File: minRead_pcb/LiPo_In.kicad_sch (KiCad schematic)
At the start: 2 parts, among them J5 Conn_01x02, Q3 IRLML6402

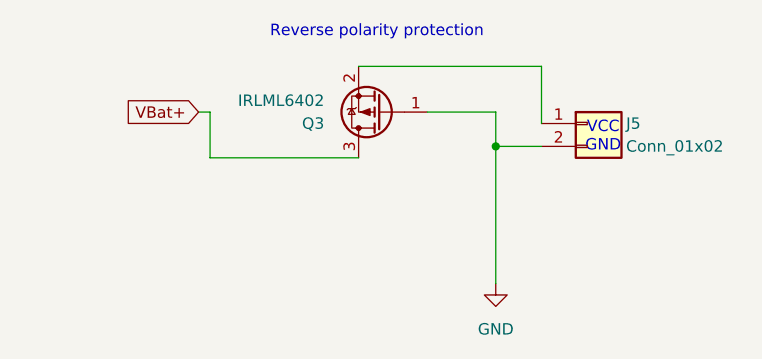
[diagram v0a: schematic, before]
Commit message: - schematic updates: - usb500 mode enabled on bq - charge limit set to 100mA 8.9kohm (safe for small batteries) - series resistors on sd card and epd lines - esd arrays for usb-c and sd-card - increased output cap for ldo from 4.7u to 22u - added pgood to gpio - confirmed reverse polarity stuff - cap to ground instead of series for sd card vdd - fixed cap values on epd
new layout:
- adjusted board size
- very compact
- need to fill ground planes and check drc errors (a lot because of solder mask)
- need to adjust jst footprint in case there's a better choice
- review review review
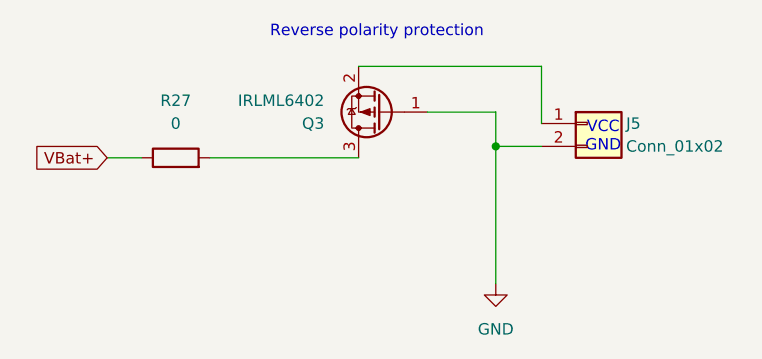
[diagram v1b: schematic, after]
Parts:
- added R27: 0, Resistor_SMD:R_0603_1608Metric_Pad0.98x0.95mm_HandSolder, symbol Device:R
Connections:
- net VBat+: now also R27.1; no longer Q3.3 (D)
- new net: Q3.3 (D), R27.2
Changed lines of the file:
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@@
-	(wire
-		(pts
-			(xy 123.19 93.98) (xy 106.68 93.98)
-		)
-		(stroke
-			(width 0)
-			(type default)
-		)
-	)
 	(wire
 		(pts
@@
 	(wire
 		(pts
+			(xy 95.25 93.98) (xy 99.06 93.98)
+		)
+		(stroke
+			(width 0)
+			(type default)
+		)
+	)
+	(wire
+		(pts
 			(xy 143.51 92.71) (xy 138.43 92.71)
 		)
@@
 	(wire
 		(pts
-			(xy 106.68 93.98) (xy 106.68 88.9)
-		)
-		(stroke
-			(width 0)
-			(type default)
-		)
-	)
-	(wire
-		(pts
-			(xy 106.68 88.9) (xy 105.41 88.9)
+			(xy 106.68 93.98) (xy 123.19 93.98)
 		)
 		(stroke
@@
 	(global_label "VBat+"
 		(shape input)
-		(at 105.41 88.9 180)
+		(at 95.25 93.98 180)
 		(fields_autoplaced yes)
 		(effects
@@
 		)
 		(property "Intersheetrefs" "${INTERSHEET_REFS}"
-			(at 96.6191 88.9 0)
+			(at 86.4591 93.98 0)
 			(effects
 				(font
@@
 					(unit 1)
 				)
+			)
+		)
+	)
+	(symbol
+		(lib_id "Device:R")
+		(at 102.87 93.98 90)
+		(unit 1)
+		(exclude_from_sim no)
+		(in_bom yes)
+		(on_board yes)
+		(dnp no)
+		(fields_autoplaced yes)
+		(property "Reference" "R27"
+			(at 102.87 87.63 90)
+			(effects
+				(font
+					(size 1.27 1.27)
+				)
+			)
+		)
+		(property "Value" "0"
+			(at 102.87 90.17 90)
+			(effects
+				(font
+					(size 1.27 1.27)
+				)
+			)
+		)
+		(property "Footprint" "Resistor_SMD:R_0603_1608Metric_Pad0.98x0.95mm_HandSolder"
+			(at 102.87 95.758 90)
+			(effects
+				(font
+					(size 1.27 1.27)
+				)
+				(hide yes)
+			)
+		)
+		(property "Datasheet" "~"
+			(at 102.87 93.98 0)
+			(effects
+				(font
+					(size 1.27 1.27)
+				)
+				(hide yes)
+			)
+		)
+		(property "Description" "Resistor"
+			(at 102.87 93.98 0)
+			(effects
+				(font
+					(size 1.27 1.27)
+				)
+				(hide yes)
+			)
+		)
+		(pin "1"
+		)
+		(pin "2"
+		)
+		(instances
+			(project ""
+				(path "/2fbd4c8f-b784-4d80-b374-4947df99a9bf/09cb559b-edfe-4b7a-bf48-944d2ba9ecd0"
+					(reference "R27")
+					(unit 1)
+				)

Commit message: draft1.0
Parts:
- R27: footprint Resistor_SMD:R_0603_1608Metric_Pad0.98x0.95mm_HandSolder -> Resistor_SMD:R_0805_2012Metric_Pad1.20x1.40mm_HandSolder
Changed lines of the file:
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@@
 			)
 		)
-		(property "Footprint" "Resistor_SMD:R_0603_1608Metric_Pad0.98x0.95mm_HandSolder"
+		(property "Footprint" "Resistor_SMD:R_0805_2012Metric_Pad1.20x1.40mm_HandSolder"
 			(at 102.87 95.758 90)
 			(effects

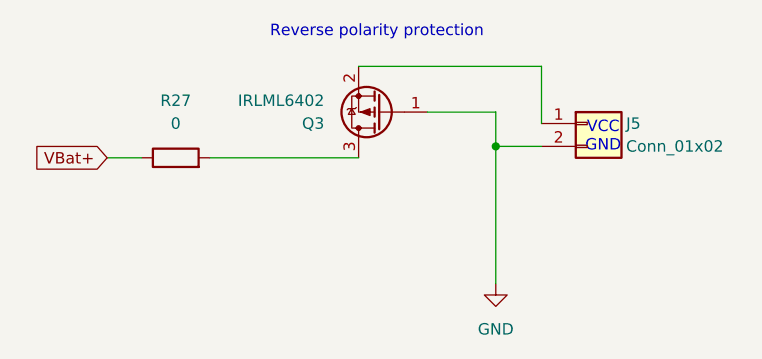
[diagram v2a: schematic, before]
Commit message: - fixed diode orientation of eink booster - everything works except eink driver: - rst pin pulls high, dc doesn't toggle, etc etc. - TODO for next rev: - remove reset stabilizer and just route 3v3 to epd inductor circuit - replace esd arrays with hand-solderable components (qfn to sot) - replace buttons with resistor ladder circuit (xteink-like) - replace bq24074 with more discrete charging circuit to aid hand-solder - add led driver (15v to 7 series LEDs) - replace usb-c receptacle with through-hole - add external dupont pins for external LED driver access and spare GPIOs
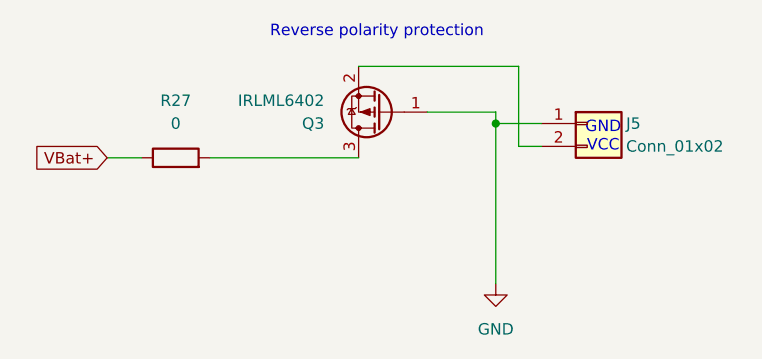
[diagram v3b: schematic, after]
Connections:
- net GND: now also J5.1 (Pin_1); no longer J5.2 (Pin_2)
- net at Q3.2 (S): now also J5.2 (Pin_2); no longer J5.1 (Pin_1)
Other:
- note added: "GND VCC"
- note removed: "VCC GND"
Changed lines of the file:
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@@
 		)
 	)
-	(text "VCC\nGND"
+	(text "GND\nVCC"
 		(exclude_from_sim no)
 		(at 150.368 91.694 0)
@@
 	)
 	(junction
-		(at 138.43 92.71)
+		(at 138.43 90.17)
 		(diameter 0)
 		(color 0 0 0 0)
@@
 	(wire
 		(pts
-			(xy 123.19 83.82) (xy 143.51 83.82)
+			(xy 123.19 83.82) (xy 140.97 83.82)
+		)
+		(stroke
+			(width 0)
+			(type default)
+		)
+	)
+	(wire
+		(pts
+			(xy 138.43 90.17) (xy 138.43 107.95)
 		)
 		(stroke
@@
 	(wire
 		(pts
-			(xy 143.51 83.82) (xy 143.51 90.17)
+			(xy 140.97 83.82) (xy 140.97 92.71)
 		)
 		(stroke
@@
 	(wire
 		(pts
-			(xy 143.51 92.71) (xy 138.43 92.71)
+			(xy 140.97 92.71) (xy 143.51 92.71)
 		)
 		(stroke
@@
 	(wire
 		(pts
-			(xy 138.43 88.9) (xy 138.43 92.71)
+			(xy 143.51 90.17) (xy 138.43 90.17)
 		)
 		(stroke
@@
 	(wire
 		(pts
-			(xy 138.43 92.71) (xy 138.43 107.95)
+			(xy 138.43 88.9) (xy 138.43 90.17)
 		)
 		(stroke

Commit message: gigantic commit, my bad revised schematic to sanity check turns out my fpc was flipped, now fixed added following schematics: - battery protection circuit - series LED driver - external peripheral connector for unused GPIO revised following schematics: - power path, replaced with mcp charger and FET rather than bq - buttons, opted for resistor ladder circuit, added two more for xte compatibility - eink driver, opted to change to updated components from waveshare 2.3 - updated esd components for usb-c and sdmmc - updated usb-c receptacle, now through-hole
New layout:
- mostly same as last time, but work done to ensure good grounding for LED/eink circuits
- eink gpio has minimal crossing/coupling just in case
- esp32 and 24 pin headers have longer pads hopefully for easier soldering
- external header in corner back of device
- prettier passive component layout
- fat 3v3 traces and small zone fill

- todo:
- DRC errors, mostly clearance and silkscreen overlap
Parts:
- removed J5: Conn_01x02, Connector_JST:JST_PH_S2B-PH-K_1x02_P2.00mm_Horizontal, symbol Connector_Generic:Conn_01x02
- removed Q3: IRLML6402, Package_TO_SOT_SMD:SOT-23_Handsoldering, symbol Transistor_FET:IRLML6402
- removed R27: 0, Resistor_SMD:R_0805_2012Metric_Pad1.20x1.40mm_HandSolder, symbol Device:R
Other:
- note removed: "GND VCC"
- note removed: "Reverse polarity protection"
